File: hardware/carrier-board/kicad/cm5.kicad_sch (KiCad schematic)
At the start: 0 parts

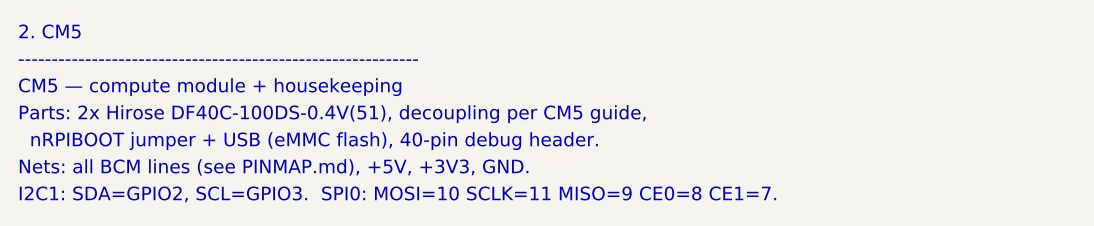
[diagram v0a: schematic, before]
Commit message: Carrier docs + KiCad plan: full two-brain pass (CM5 HUB75 + RP2354B I/O)
Propagate the two-brain architecture across the whole doc set and KiCad plan:
- REQUIREMENTS: restructured M1-M12 (CM5 HUB75; RP2354B core/MAX7219/WS2812/
  sensors/buttons/servos; USB selector + standalone program port); N-list reworked.
- POWER: add +V_SERVO and +3V3_RP rails, servo current budget, updated worked
  total + protection; sensors now on +3V3_RP not CM5 3V3.
- CONNECTORS: J3 re-sourced to RP2354B SPI0, J4 4 WS2812 zones, J5 +SENS_INT,
  J6 BTN1..10, add J12 USB-C, J20-J27 servos, SW1 USB selector, SWD/UART hdrs;
  drop JP1/JP2; fans presented as RP2354B-default-or-CM5 (decision flagged).
- BOM: add RP2354B core, '125/'245 (RP side), USB mux/USB-C/ESD, servo headers,
  +3V3_RP reg; fix '125 double-count and stale HUB75/MAX7219-shared-buffer/JP1.
- MULTI-BACKEND: HUB75+MAX7219 now simultaneous (different brains); firmware
  CompositePanelOutput is the sole remaining blocker.
- IO-EXPANSION: RP2354B is the primary I/O backbone; I2C expanders secondary.
- kicad: 11-sheet plan, stable UUIDs, generator skips populated face_buffer.
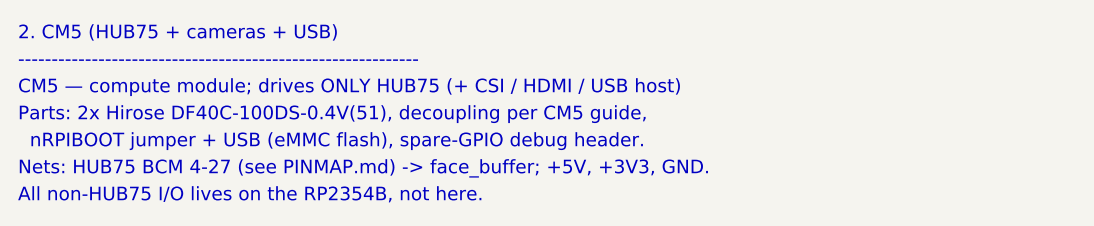
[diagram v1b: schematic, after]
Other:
- note added: "2. CM5 (HUB75 + cameras + USB)"
- note added: "All non-HUB75 I/O lives on the RP2354B, not here."
- note added: "CM5 — compute module; drives ONLY HUB75 (+ CSI / HDMI / USB host)"
- note added: "Nets: HUB75 BCM 4-27 (see PINMAP.md) -> face_buffer; +5V, +3V3, GND."
- note added: "nRPIBOOT jumper + USB (eMMC flash), spare-GPIO debug header."
- note removed: "2. CM5"
- note removed: "CM5 — compute module + housekeeping"
- note removed: "I2C1: SDA=GPIO2, SCL=GPIO3. SPI0: MOSI=10 SCLK=11 MISO=9 CE0=8 CE1=7."
- note removed: "Nets: all BCM lines (see PINMAP.md), +5V, +3V3, GND."
- note removed: "nRPIBOOT jumper + USB (eMMC flash), 40-pin debug header."
- title: ProtoHUD Carrier — 2. CM5 -> ProtoHUD Carrier — 2. CM5 (HUB75 + cameras + USB)
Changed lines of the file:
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@@
   (paper "A3")
   (title_block
-    (title "ProtoHUD Carrier — 2. CM5")
+    (title "ProtoHUD Carrier — 2. CM5 (HUB75 + cameras + USB)")
     (rev "A")
     (company "ProtoHUD")
   )
-  (text "2. CM5" (at 25.4 25.40 0) (effects (font (size 1.5 1.5)) (justify left bottom)))
+  (text "2. CM5 (HUB75 + cameras + USB)" (at 25.4 25.40 0) (effects (font (size 1.5 1.5)) (justify left bottom)))
   (text "------------------------------------------------------------" (at 25.4 28.40 0) (effects (font (size 1.5 1.5)) (justify left bottom)))
-  (text "CM5 — compute module + housekeeping" (at 25.4 31.40 0) (effects (font (size 1.5 1.5)) (justify left bottom)))
+  (text "CM5 — compute module; drives ONLY HUB75 (+ CSI / HDMI / USB host)" (at 25.4 31.40 0) (effects (font (size 1.5 1.5)) (justify left bottom)))
   (text "Parts: 2x Hirose DF40C-100DS-0.4V(51), decoupling per CM5 guide," (at 25.4 34.40 0) (effects (font (size 1.5 1.5)) (justify left bottom)))
-  (text "  nRPIBOOT jumper + USB (eMMC flash), 40-pin debug header." (at 25.4 37.40 0) (effects (font (size 1.5 1.5)) (justify left bottom)))
-  (text "Nets: all BCM lines (see PINMAP.md), +5V, +3V3, GND." (at 25.4 40.40 0) (effects (font (size 1.5 1.5)) (justify left bottom)))
-  (text "I2C1: SDA=GPIO2, SCL=GPIO3.  SPI0: MOSI=10 SCLK=11 MISO=9 CE0=8 CE1=7." (at 25.4 43.40 0) (effects (font (size 1.5 1.5)) (justify left bottom)))
+  (text "  nRPIBOOT jumper + USB (eMMC flash), spare-GPIO debug header." (at 25.4 37.40 0) (effects (font (size 1.5 1.5)) (justify left bottom)))
+  (text "Nets: HUB75 BCM 4-27 (see PINMAP.md) -> face_buffer; +5V, +3V3, GND." (at 25.4 40.40 0) (effects (font (size 1.5 1.5)) (justify left bottom)))
+  (text "All non-HUB75 I/O lives on the RP2354B, not here." (at 25.4 43.40 0) (effects (font (size 1.5 1.5)) (justify left bottom)))
   (sheet_instances
     (path "/" (page "1"))

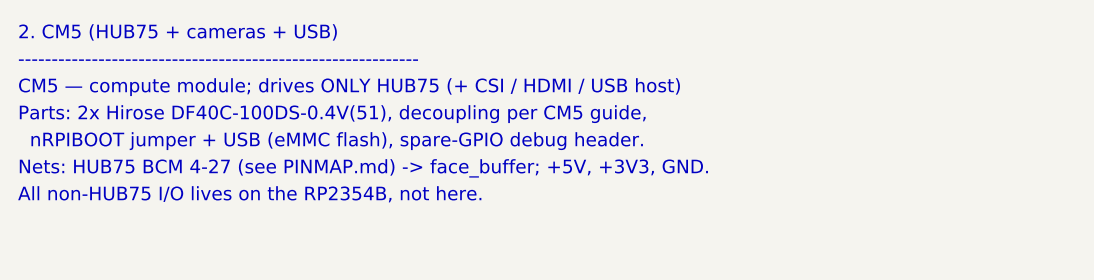
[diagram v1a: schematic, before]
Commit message: Carrier: fans are CM5-local (decision)
Lock fan control to the CM5 (sys::FanController on BCM 18/19) rather than the
RP2354B, so cooling survives a USB-link hang and reuses existing firmware.
Update CONNECTORS (fan section), REQUIREMENTS N4, PINMAP (CM5 non-HUB75 lines),
GPIO-MAP (BCM18/19 = fans, CM5 free now 8 lines; RP2354B GP38/39 plain spare),
and the cm5 KiCad stub.
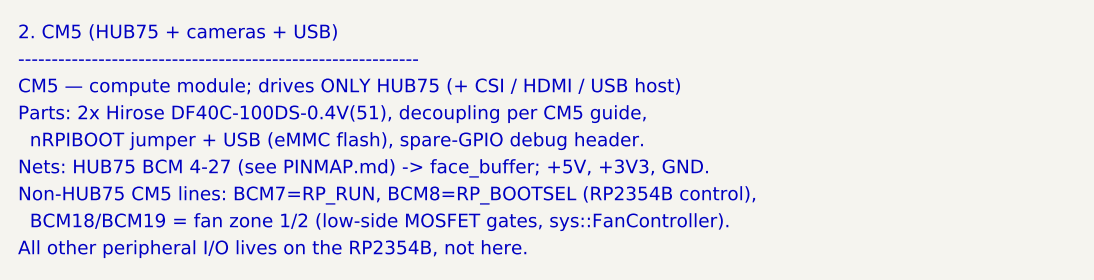
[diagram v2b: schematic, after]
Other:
- note added: "All other peripheral I/O lives on the RP2354B, not here."
- note added: "BCM18/BCM19 = fan zone 1/2 (low-side MOSFET gates, sys::FanController)."
- note added: "Non-HUB75 CM5 lines: BCM7=RP_RUN, BCM8=RP_BOOTSEL (RP2354B control),"
- note removed: "All non-HUB75 I/O lives on the RP2354B, not here."
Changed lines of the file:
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@@
   (text "  nRPIBOOT jumper + USB (eMMC flash), spare-GPIO debug header." (at 25.4 37.40 0) (effects (font (size 1.5 1.5)) (justify left bottom)))
   (text "Nets: HUB75 BCM 4-27 (see PINMAP.md) -> face_buffer; +5V, +3V3, GND." (at 25.4 40.40 0) (effects (font (size 1.5 1.5)) (justify left bottom)))
-  (text "All non-HUB75 I/O lives on the RP2354B, not here." (at 25.4 43.40 0) (effects (font (size 1.5 1.5)) (justify left bottom)))
+  (text "Non-HUB75 CM5 lines: BCM7=RP_RUN, BCM8=RP_BOOTSEL (RP2354B control)," (at 25.4 43.40 0) (effects (font (size 1.5 1.5)) (justify left bottom)))
+  (text "  BCM18/BCM19 = fan zone 1/2 (low-side MOSFET gates, sys::FanController)." (at 25.4 46.40 0) (effects (font (size 1.5 1.5)) (justify left bottom)))
+  (text "All other peripheral I/O lives on the RP2354B, not here." (at 25.4 49.40 0) (effects (font (size 1.5 1.5)) (justify left bottom)))
   (sheet_instances
     (path "/" (page "1"))

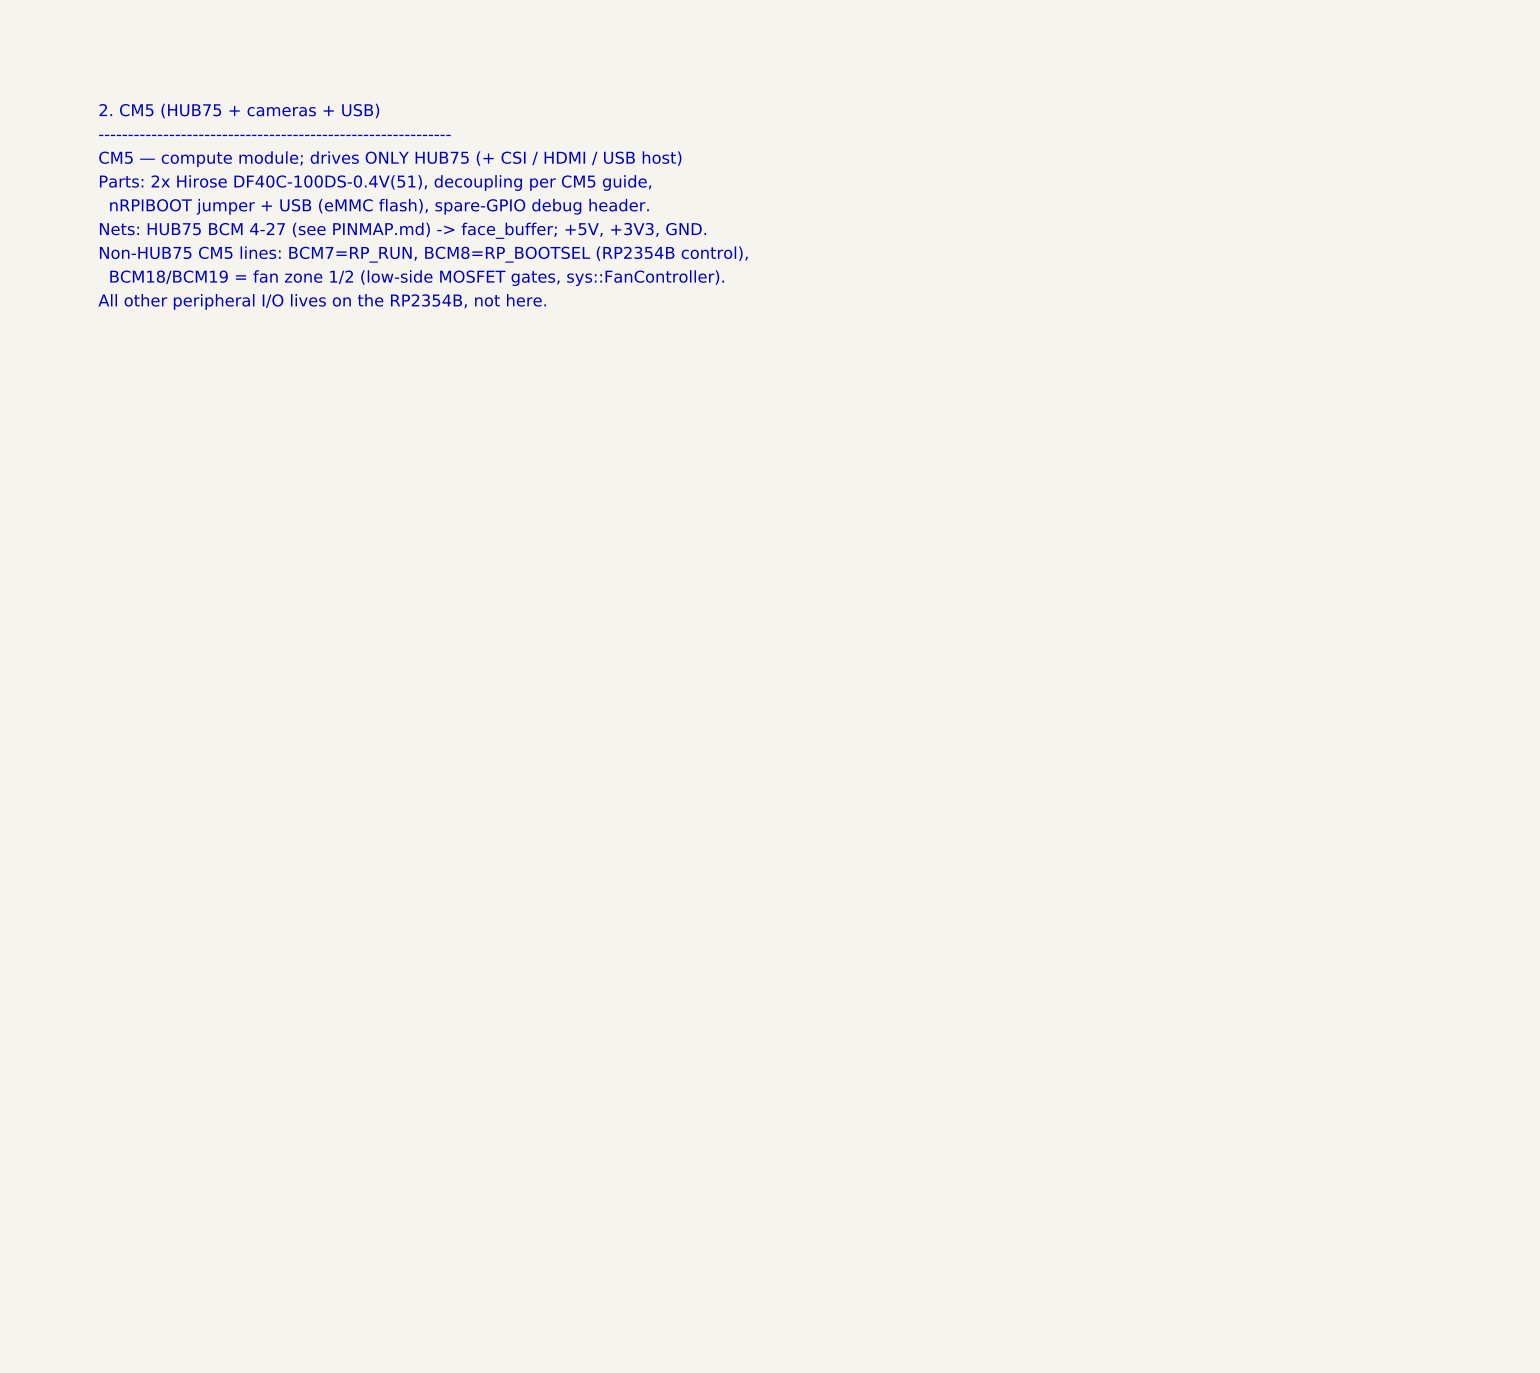
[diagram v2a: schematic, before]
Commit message: Carrier KiCad: populate all 11 schematic sheets
Replace populate_face_buffer.py with populate_sheets.py: one generator that
emits all 11 populated sub-sheets reusing the KiCad-9 format proven by the
face_buffer proof. Shared symbol library + generic box-symbol builder; condensed
CM5 (2x DF40-100) and RP2354B (QFN-80) symbols showing only used pins.

Connectivity by net labels (global for rails + cross-sheet nets: GPIOxx HUB75,
MX_*, LED*_DAT, SRV*, BTN*, *_USB_*; local within-sheet). Sheets: power
(protection + rails + AP2112 +3V3_RP), cm5 (HUB75 out + fan MOSFETs + RP ctrl),
face_buffer, rp2354_io (RP2354B + xtal + SW1/J12 + ESD + SWD), rp2354_face
(U10->J3), leds (U11 quad ->J4a-d), sensors_i2c (pull-ups+J5+STEMMA),
servos (J20-27 + rail), gpio_buttons (J6), usb (USB2514B hub + uplink),
cameras_display (CSI FFC + HDMI).

Verified: all sheets paren-balanced, every used lib_id defined, all instance
paths match sheet UUIDs, root<->sub-sheet UUID linkage intact. generate_skeleton.py
now lists all sheets POPULATED (writes only root+project). Not yet opened in
KiCad here -- expect ERC warnings (PWR_FLAG, unconnected pins) to clean.
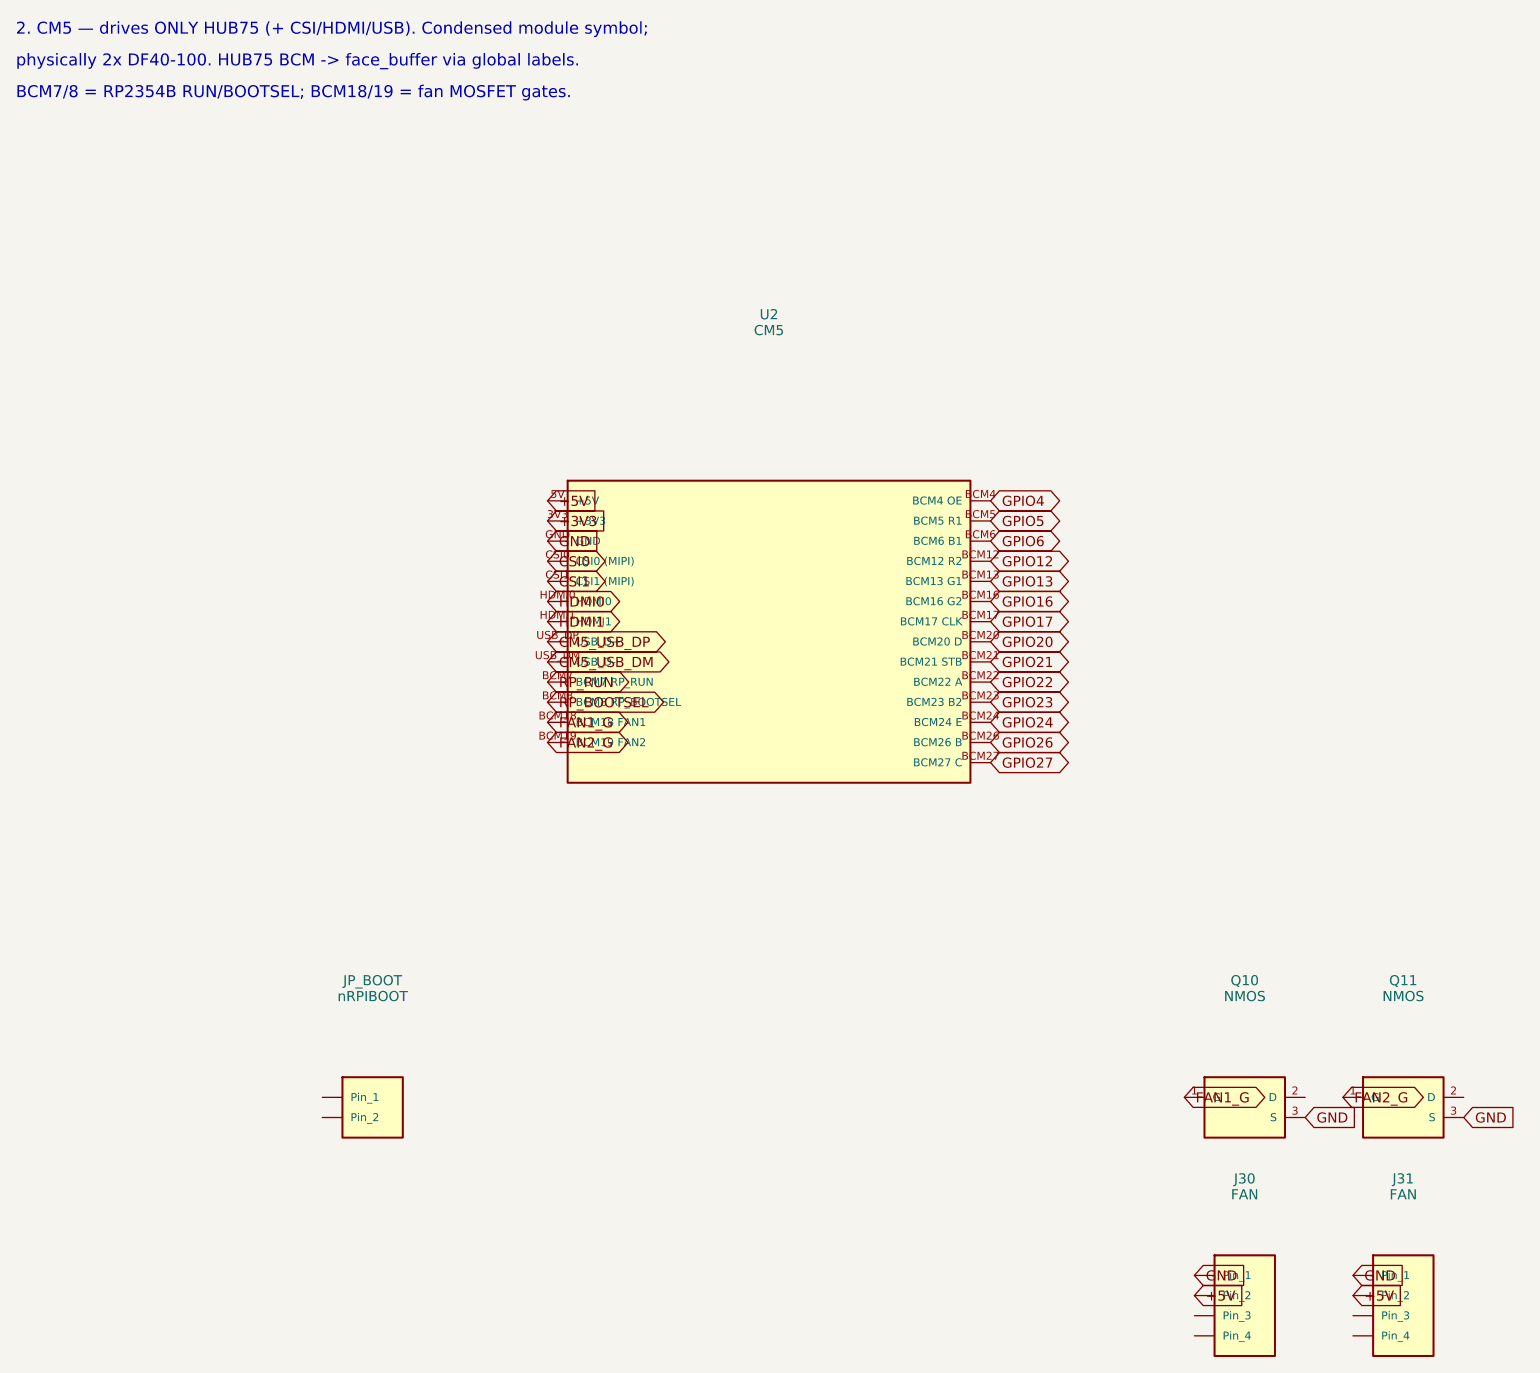
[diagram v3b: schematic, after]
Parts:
- added J30, J31: FAN, symbol Connector_Generic:Conn_01x04
- added JP_BOOT: nRPIBOOT, symbol Connector_Generic:Conn_01x02
- added Q10, Q11: NMOS, symbol Device:Q_NMOS_GSD
- added U2: CM5, symbol Module:RaspberryPi_CM5
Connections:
- new net +3V3: U2.3V3 (+3V3)
- new net +5V: J30.2 (Pin_2), J31.2 (Pin_2), U2.5V (+5V)
- new net CM5_USB_DM: U2.USB_DM (USB_D-)
- new net CM5_USB_DP: U2.USB_DP (USB_D+)
- new net CSI0: U2.CSI0 (CSI0 (MIPI))
- new net CSI1: U2.CSI1 (CSI1 (MIPI))
- new net FAN1_G: Q10.1 (G), U2.BCM18 (BCM18 FAN1)
- new net FAN2_G: Q11.1 (G), U2.BCM19 (BCM19 FAN2)
- new net GND: J30.1 (Pin_1), J31.1 (Pin_1), Q10.3 (S), Q11.3 (S), U2.GND
- new net GPIO12: U2.BCM12 (BCM12 R2)
- new net GPIO13: U2.BCM13 (BCM13 G1)
- new net GPIO16: U2.BCM16 (BCM16 G2)
- new net GPIO17: U2.BCM17 (BCM17 CLK)
- new net GPIO20: U2.BCM20 (BCM20 D)
- new net GPIO21: U2.BCM21 (BCM21 STB)
- new net GPIO22: U2.BCM22 (BCM22 A)
- new net GPIO23: U2.BCM23 (BCM23 B2)
- new net GPIO24: U2.BCM24 (BCM24 E)
- new net GPIO26: U2.BCM26 (BCM26 B)
- new net GPIO27: U2.BCM27 (BCM27 C)
- new net GPIO4: U2.BCM4 (BCM4 OE)
- new net GPIO5: U2.BCM5 (BCM5 R1)
- new net GPIO6: U2.BCM6 (BCM6 B1)
- new net HDMI0: U2.HDMI0
- new net HDMI1: U2.HDMI1
- new net RP_BOOTSEL: U2.BCM8 (BCM8 RP_BOOTSEL)
- new net RP_RUN: U2.BCM7 (BCM7 RP_RUN)
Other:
- note added: "2. CM5 — drives ONLY HUB75 (+ CSI/HDMI/USB). Condensed module symbol;"
- note added: "BCM7/8 = RP2354B RUN/BOOTSEL; BCM18/19 = fan MOSFET gates."
- note added: "physically 2x DF40-100. HUB75 BCM -> face_buffer via global labels."
- note removed: "------------------------------------------------------------"
- note removed: "2. CM5 (HUB75 + cameras + USB)"
- note removed: "All other peripheral I/O lives on the RP2354B, not here."
- note removed: "BCM18/BCM19 = fan zone 1/2 (low-side MOSFET gates, sys::FanController)."
- note removed: "CM5 — compute module; drives ONLY HUB75 (+ CSI / HDMI / USB host)"
- note removed: "Nets: HUB75 BCM 4-27 (see PINMAP.md) -> face_buffer; +5V, +3V3, GND."
- note removed: "Non-HUB75 CM5 lines: BCM7=RP_RUN, BCM8=RP_BOOTSEL (RP2354B control),"
- note removed: "Parts: 2x Hirose DF40C-100DS-0.4V(51), decoupling per CM5 guide,"
- note removed: "nRPIBOOT jumper + USB (eMMC flash), spare-GPIO debug header."
